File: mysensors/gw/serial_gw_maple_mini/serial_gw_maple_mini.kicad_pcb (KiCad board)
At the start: 2 copper layers, 70 x 50 mm, 349 parts, among them U1 MAPLEMINI, U2 AMS1117-3.3, U3 E01-ML01DP5

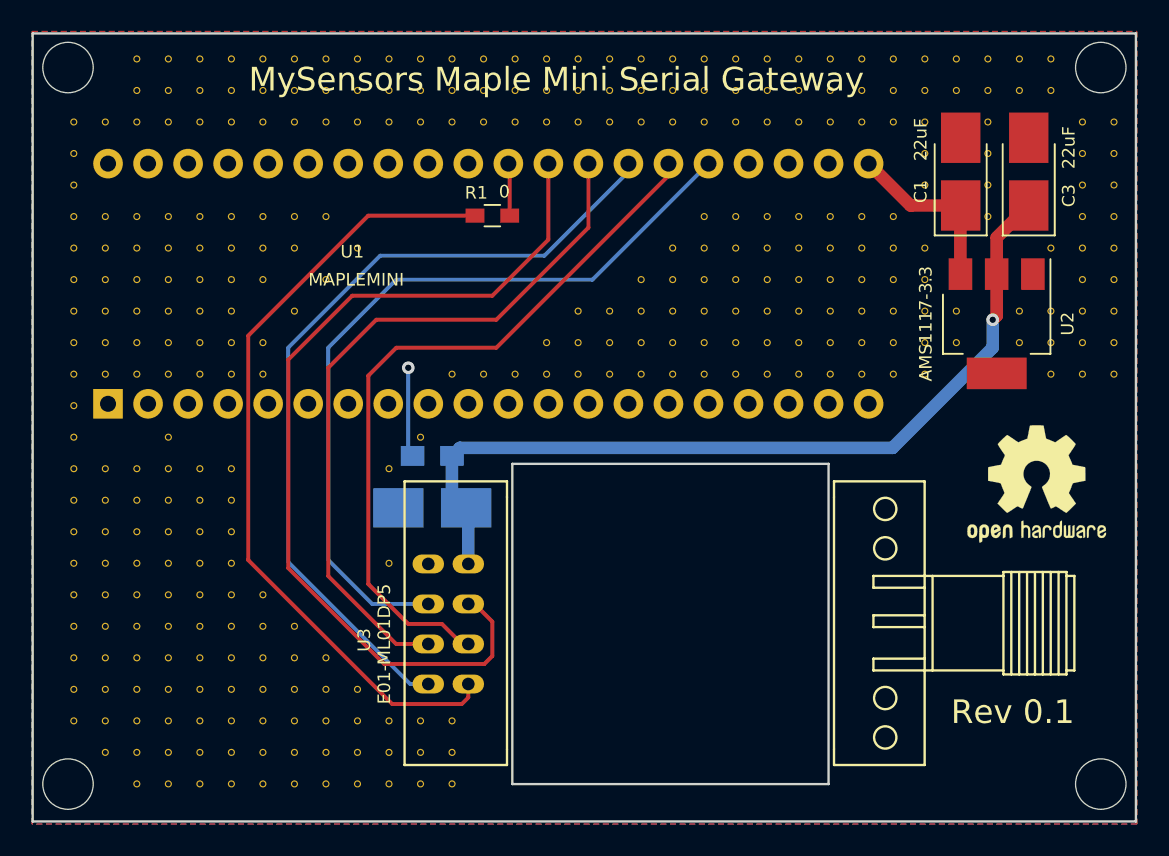
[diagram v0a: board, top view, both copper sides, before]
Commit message: oval pads for maple mini footprint as it allows tracks easily between
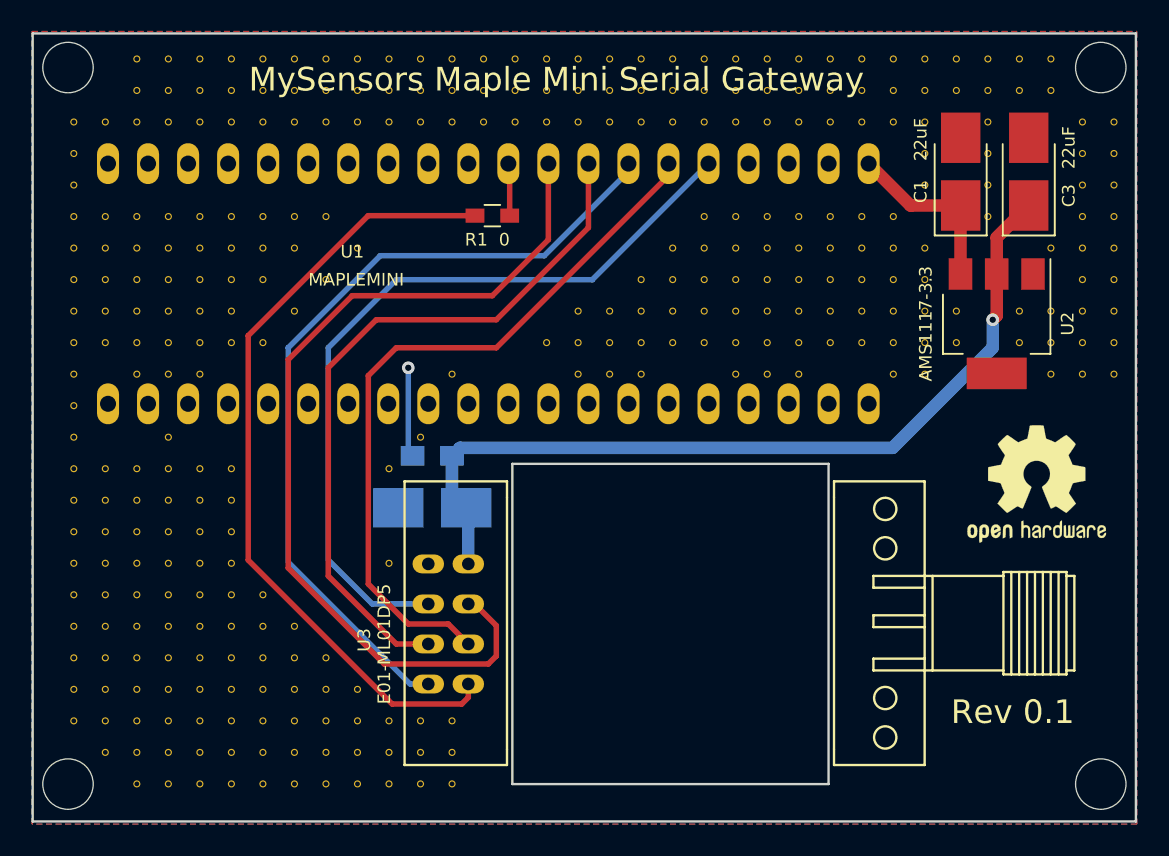
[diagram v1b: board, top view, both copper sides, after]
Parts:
- removed V10_13, V11_13, V18_13, V19_13, V20_13, V24_13, V25_13, V29_13, V30_13, V6_13: AUTO_VIA, VIA_MATRIX

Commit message: serial_gw maple_mini final touches
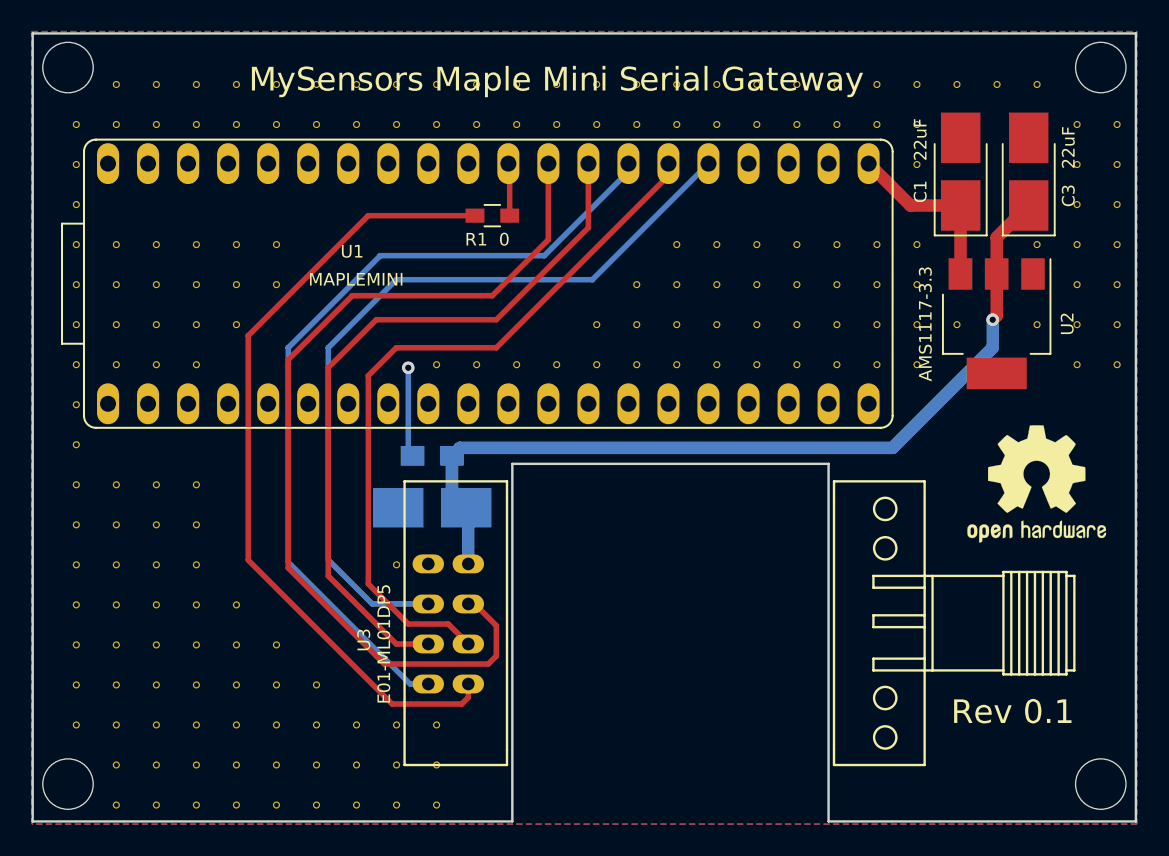
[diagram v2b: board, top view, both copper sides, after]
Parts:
- removed V10_10, V10_11, V10_12, V10_16, V10_17, V10_22, V10_23, V10_24, V10_25, V10_26, V10_5, V10_8, V10_9, V11_10, V11_12, V11_22, V11_23, V11_24, V11_25, V11_26, V11_5, V11_8, V11_9, V12_11, V12_22, V12_23, V12_24, V12_25, V12_26, V12_5, V12_8, V12_9, V13_22, V13_23, V13_24, V13_25, V13_26, V13_5, V13_8, V14_23, V14_24, V14_25, V14_26, V14_5, V14_9, V15_16, V15_19, V15_24, V15_25, V15_26, V15_5, V16_15, V16_24, V16_25, V16_26, V16_5, V17_13, V17_24, V17_25, V17_26, V17_5, V18_5, V19_5, V20_12, V20_5, V21_11, V21_12, V21_13, V21_5, V22_11, V22_12, V22_13, V22_5, V23_11, V23_12, V23_13, V23_5, V24_11, V24_12, V24_5, V25_11, V25_12, V26_10, V26_11, V26_12, V26_13, V26_4, V26_5, V26_8, V27_10, V27_11, V27_12, V27_13, V27_4, V27_5, V27_8, V27_9, V28_10, V28_11, V28_12, V28_13, V28_4, V28_5, V28_8, V29_11, V29_12, V29_3, V30_11, V30_12, V30_3, V31_10, V31_11, V31_12, V31_13, V31_3, V31_4, V31_5, V31_8, V31_9, V32_10, V32_11, V32_12, V32_13, V32_3, V32_4, V32_5, V32_6, V32_7, V32_9, V33_11, V33_12, V33_3, V33_4, V34_3, V34_4, V34_5, V34_6, V34_7, V34_8, V35_11, V35_12, V35_3, V35_4, V36_11, V36_12, V36_13, V36_3, V36_4, V36_9, V37_10, V37_11, V37_12, V37_13, V37_5, V37_6, V37_7, V37_8, V37_9, V38_10, V38_11, V38_12, V38_13, V38_5, V38_6, V38_7, V38_8, V38_9, V5_11, V5_12, V5_22, V5_23, V5_24, V5_5, V5_6, V6_11, V6_12, V6_22, V6_23, V6_24, V6_25, V6_5, V7_11, V7_12, V7_22, V7_23, V7_24, V7_25, V7_26, V7_5, V8_10, V8_11, V8_12, V8_13, V8_15, V8_22, V8_23, V8_24, V8_25, V8_26, V8_5, V9_10, V9_11, V9_12, V9_13, V9_16, V9_22, V9_23, V9_24, V9_25, V9_26, V9_5, V9_9: AUTO_VIA, VIA_MATRIX
- added V11_19: AUTO_VIA, VIA_MATRIX, F.Cu at (160.5, 83.9)
- added V12_15: AUTO_VIA, VIA_MATRIX, F.Cu at (163.1, 73.7)
- added V12_19: AUTO_VIA, VIA_MATRIX, F.Cu at (163.1, 83.9)
- added V12_20: AUTO_VIA, VIA_MATRIX, F.Cu at (163.1, 86.4)
- added V13_19: AUTO_VIA, VIA_MATRIX, F.Cu at (165.6, 83.9)
- added V13_20: AUTO_VIA, VIA_MATRIX, F.Cu at (165.6, 86.4)
- added V13_21: AUTO_VIA, VIA_MATRIX, F.Cu at (165.6, 89.0)
- added V14_10: AUTO_VIA, VIA_MATRIX, F.Cu at (168.2, 61.0)
- added V15_10: AUTO_VIA, VIA_MATRIX, F.Cu at (170.7, 61.0)
- added V16_10: AUTO_VIA, VIA_MATRIX, F.Cu at (173.2, 61.0)
- added V17_10: AUTO_VIA, VIA_MATRIX, F.Cu at (175.8, 61.0)
- added V17_9: AUTO_VIA, VIA_MATRIX, F.Cu at (175.8, 58.5)
- added V18_10: AUTO_VIA, VIA_MATRIX, F.Cu at (178.3, 61.0)
- added V18_8: AUTO_VIA, VIA_MATRIX, F.Cu at (178.3, 55.9)
- added V18_9: AUTO_VIA, VIA_MATRIX, F.Cu at (178.3, 58.5)
- added V19_10: AUTO_VIA, VIA_MATRIX, F.Cu at (180.9, 61.0)
- added V19_7: AUTO_VIA, VIA_MATRIX, F.Cu at (180.9, 53.4)
- added V19_8: AUTO_VIA, VIA_MATRIX, F.Cu at (180.9, 55.9)
- added V19_9: AUTO_VIA, VIA_MATRIX, F.Cu at (180.9, 58.5)
- added V20_10: AUTO_VIA, VIA_MATRIX, F.Cu at (183.4, 61.0)
- added V20_7: AUTO_VIA, VIA_MATRIX, F.Cu at (183.4, 53.4)
- added V20_8: AUTO_VIA, VIA_MATRIX, F.Cu at (183.4, 55.9)
- added V20_9: AUTO_VIA, VIA_MATRIX, F.Cu at (183.4, 58.5)
- added V21_10: AUTO_VIA, VIA_MATRIX, F.Cu at (185.9, 61.0)
- added V21_7: AUTO_VIA, VIA_MATRIX, F.Cu at (185.9, 53.4)
- added V21_8: AUTO_VIA, VIA_MATRIX, F.Cu at (185.9, 55.9)
- added V21_9: AUTO_VIA, VIA_MATRIX, F.Cu at (185.9, 58.5)
- added V22_10: AUTO_VIA, VIA_MATRIX, F.Cu at (188.5, 61.0)
- added V22_7: AUTO_VIA, VIA_MATRIX, F.Cu at (188.5, 53.4)
- added V22_8: AUTO_VIA, VIA_MATRIX, F.Cu at (188.5, 55.9)
- added V22_9: AUTO_VIA, VIA_MATRIX, F.Cu at (188.5, 58.5)
- added V23_7: AUTO_VIA, VIA_MATRIX, F.Cu at (191.0, 53.4)
- added V23_8: AUTO_VIA, VIA_MATRIX, F.Cu at (191.0, 55.9)
- added V23_9: AUTO_VIA, VIA_MATRIX, F.Cu at (191.0, 58.5)
- added V24_7: AUTO_VIA, VIA_MATRIX, F.Cu at (193.6, 53.4)
- added V24_8: AUTO_VIA, VIA_MATRIX, F.Cu at (193.6, 55.9)
- added V25_7: AUTO_VIA, VIA_MATRIX, F.Cu at (196.1, 53.4)
- added V28_7: AUTO_VIA, VIA_MATRIX, F.Cu at (203.7, 53.4)
- added V29_6: AUTO_VIA, VIA_MATRIX, F.Cu at (206.3, 50.9)
- added V29_7: AUTO_VIA, VIA_MATRIX, F.Cu at (206.3, 53.4)
- added V30_6: AUTO_VIA, VIA_MATRIX, F.Cu at (208.8, 50.9)
- added V30_7: AUTO_VIA, VIA_MATRIX, F.Cu at (208.8, 53.4)
- added V4_10: AUTO_VIA, VIA_MATRIX, F.Cu at (142.8, 61.0)
- added V4_11: AUTO_VIA, VIA_MATRIX, F.Cu at (142.8, 63.6)
- added V4_12: AUTO_VIA, VIA_MATRIX, F.Cu at (142.8, 66.1)
- added V4_13: AUTO_VIA, VIA_MATRIX, F.Cu at (142.8, 68.6)
- added V4_14: AUTO_VIA, VIA_MATRIX, F.Cu at (142.8, 71.2)
- added V4_15: AUTO_VIA, VIA_MATRIX, F.Cu at (142.8, 73.7)
- added V4_16: AUTO_VIA, VIA_MATRIX, F.Cu at (142.8, 76.3)
- added V4_17: AUTO_VIA, VIA_MATRIX, F.Cu at (142.8, 78.8)
- added V4_18: AUTO_VIA, VIA_MATRIX, F.Cu at (142.8, 81.3)
- added V4_19: AUTO_VIA, VIA_MATRIX, F.Cu at (142.8, 83.9)
- added V4_4: AUTO_VIA, VIA_MATRIX, F.Cu at (142.8, 45.8)
- added V4_5: AUTO_VIA, VIA_MATRIX, F.Cu at (142.8, 48.3)
- added V4_6: AUTO_VIA, VIA_MATRIX, F.Cu at (142.8, 50.9)
- added V4_7: AUTO_VIA, VIA_MATRIX, F.Cu at (142.8, 53.4)
- added V4_8: AUTO_VIA, VIA_MATRIX, F.Cu at (142.8, 55.9)
- added V4_9: AUTO_VIA, VIA_MATRIX, F.Cu at (142.8, 58.5)
- added V5_3: AUTO_VIA, VIA_MATRIX, F.Cu at (145.3, 43.2)
- added V5_4: AUTO_VIA, VIA_MATRIX, F.Cu at (145.3, 45.8)
- added V6_13: AUTO_VIA, VIA_MATRIX, F.Cu at (147.8, 68.6)
- added V6_14: AUTO_VIA, VIA_MATRIX, F.Cu at (147.8, 71.2)
- added V6_15: AUTO_VIA, VIA_MATRIX, F.Cu at (147.8, 73.7)
- added V6_3: AUTO_VIA, VIA_MATRIX, F.Cu at (147.8, 43.2)
- added V6_4: AUTO_VIA, VIA_MATRIX, F.Cu at (147.8, 45.8)
- added V6_7: AUTO_VIA, VIA_MATRIX, F.Cu at (147.8, 53.4)
- added V7_14: AUTO_VIA, VIA_MATRIX, F.Cu at (150.4, 71.2)
- added V7_15: AUTO_VIA, VIA_MATRIX, F.Cu at (150.4, 73.7)
- added V7_7: AUTO_VIA, VIA_MATRIX, F.Cu at (150.4, 53.4)
- added V8_7: AUTO_VIA, VIA_MATRIX, F.Cu at (152.9, 53.4)
- added V9_7: AUTO_VIA, VIA_MATRIX, F.Cu at (155.5, 53.4)
- moved V30_10 17.1 mm to (208.8, 61.0)
- moved V30_9 16.9 mm to (208.8, 58.5)
- moved V30_8 16.8 mm to (208.8, 55.9)
- moved V29_10 16.6 mm to (206.3, 61.0)
- moved V30_5 16.4 mm to (208.8, 48.3)
- moved V29_9 16.4 mm to (206.3, 58.5)
- moved V30_4 16.3 mm to (208.8, 45.8)
- moved V29_8 16.2 mm to (206.3, 55.9)
- moved V29_5 15.9 mm to (206.3, 48.3)
- moved V28_9 15.9 mm to (203.7, 58.5)
- moved V29_4 15.8 mm to (206.3, 45.8)
- moved V28_3 15.2 mm to (203.7, 43.2)
- moved V26_9 14.9 mm to (198.6, 58.5)
- moved V27_3 14.7 mm to (201.2, 43.2)
- moved V25_10 14.5 mm to (196.1, 61.0)
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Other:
- outline, holes or cut-outs redrawn

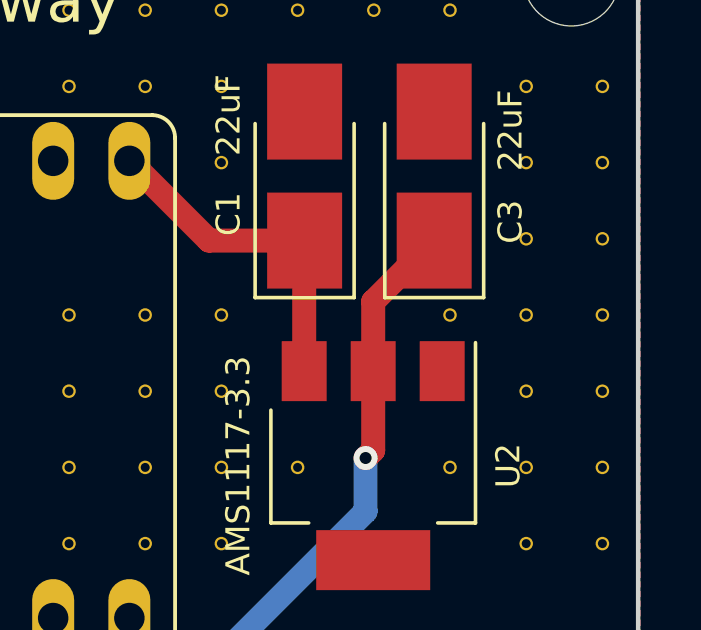
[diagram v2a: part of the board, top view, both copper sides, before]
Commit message: serial_gw maple_mini final touches
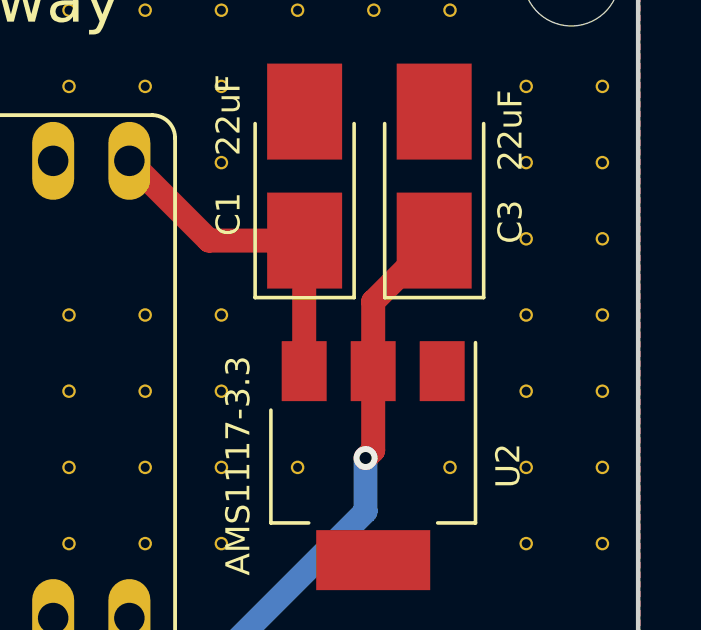
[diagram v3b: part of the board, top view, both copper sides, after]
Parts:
- removed V28_7: AUTO_VIA, VIA_MATRIX

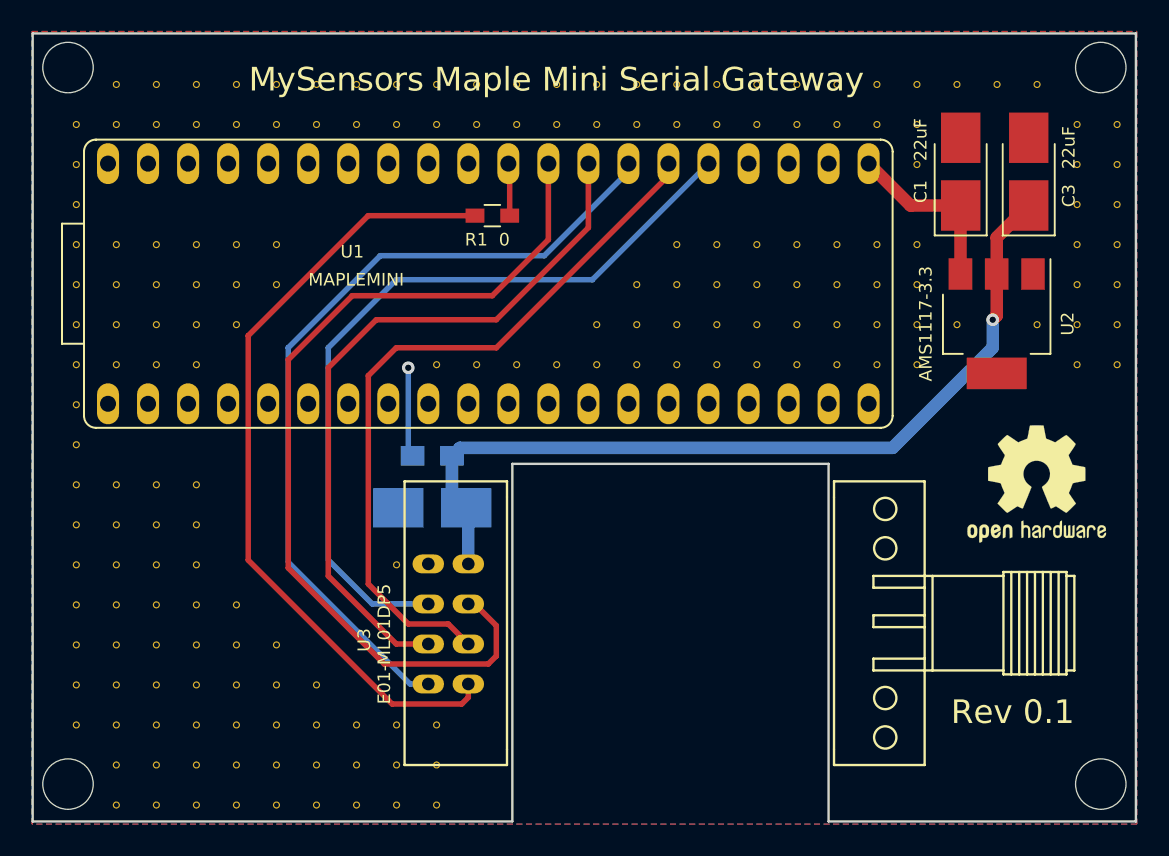
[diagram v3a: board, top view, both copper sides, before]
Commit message: serial_gw maple_mini - oops! forgot to connect common ground
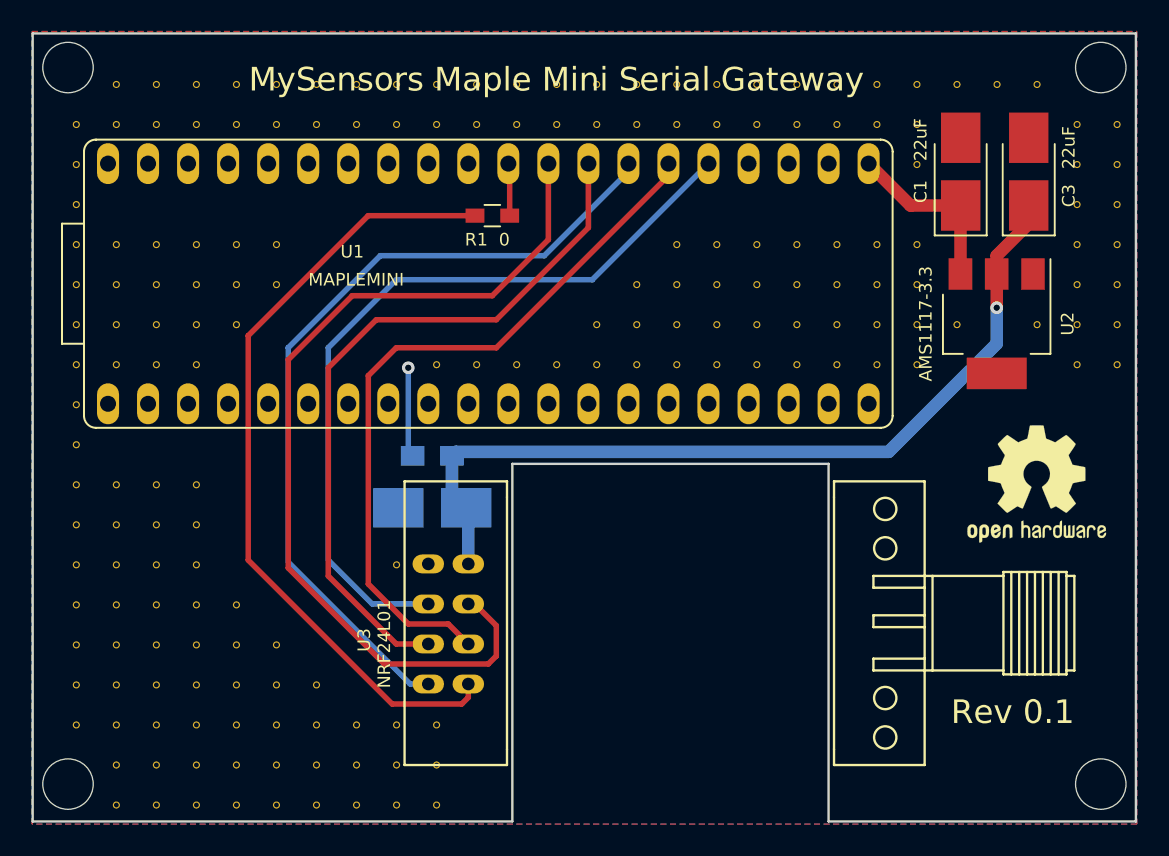
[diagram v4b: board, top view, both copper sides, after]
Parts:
- U3: value E01-ML01DP5 -> NRF24L01
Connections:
- U1 pad 1: Net-(U1-Pad1) -> (no net)
- U1 pad 10: Net-(U1-Pad10) -> (no net)
- U1 pad 11: Net-(U1-Pad11) -> (no net)
- U1 pad 12: Net-(U1-Pad12) -> (no net)
- U1 pad 13: Net-(U1-Pad13) -> (no net)
- U1 pad 14: Net-(U1-Pad14) -> (no net)
- U1 pad 15: Net-(U1-Pad15) -> (no net)
- U1 pad 16: Net-(U1-Pad16) -> (no net)
- U1 pad 17: Net-(U1-Pad17) -> (no net)
- U1 pad 18: Net-(U1-Pad18) -> (no net)
- U1 pad 19: Net-(U1-Pad19) -> (no net)
- U1 pad 2: Net-(U1-Pad2) -> GND
- U1 pad 20: Net-(U1-Pad20) -> (no net)
- U1 pad 22: Net-(U1-Pad22) -> (no net)
- U1 pad 23: Net-(U1-Pad23) -> (no net)
- U1 pad 24: Net-(U1-Pad24) -> (no net)
- U1 pad 3: Net-(U1-Pad3) -> (no net)
- U1 pad 31: Net-(U1-Pad31) -> (no net)
- U1 pad 32: Net-(U1-Pad32) -> (no net)
- U1 pad 33: Net-(U1-Pad33) -> (no net)
- U1 pad 34: Net-(U1-Pad34) -> (no net)
- U1 pad 35: Net-(U1-Pad35) -> (no net)
- U1 pad 36: Net-(U1-Pad36) -> (no net)
- U1 pad 37: Net-(U1-Pad37) -> (no net)
- U1 pad 38: Net-(U1-Pad38) -> (no net)
- U1 pad 39: Net-(U1-Pad39) -> (no net)
- U1 pad 4: Net-(U1-Pad4) -> (no net)
- U1 pad 40: Net-(U1-Pad40) -> (no net)
- U1 pad 5: Net-(U1-Pad5) -> (no net)
- U1 pad 6: Net-(U1-Pad6) -> (no net)
- U1 pad 7: Net-(U1-Pad7) -> (no net)
- U1 pad 8: Net-(U1-Pad8) -> (no net)
- U1 pad 9: Net-(U1-Pad9) -> (no net)
